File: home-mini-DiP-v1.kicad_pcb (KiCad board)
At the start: 4 copper layers, 72.4 x 70 mm, 241 parts, among them J1 FH34SRJ-16S-0.5SH_50_, J2 1775443-2, J3 XMOS JTAG, J4 XTAG DEV, J5 Conn_01x05, Q1 LBSS138WT1G, Q2 LBSS138WT1G, Q3 BC847B, SW2 BOOT, U1 AP22802AW5-7, U10 SN74LVC125APWR, U11 TLV73333PDBVR, U13 TLV320AIC3204IRHBR, U14 TPA6211A1DGNR, U2 MPR121QR2, U3 TPS62827DMQR, U4 TPS62065DSGR, U5 ME6211C18M5G-N, U6 ESP32-S3R8, U7 W25Q128JVSIQ, U8 XU316-1024-QF60B-C24​, U9 W25Q32JVSSIQ, X1 24MHz 12pF, Y1 40MHz

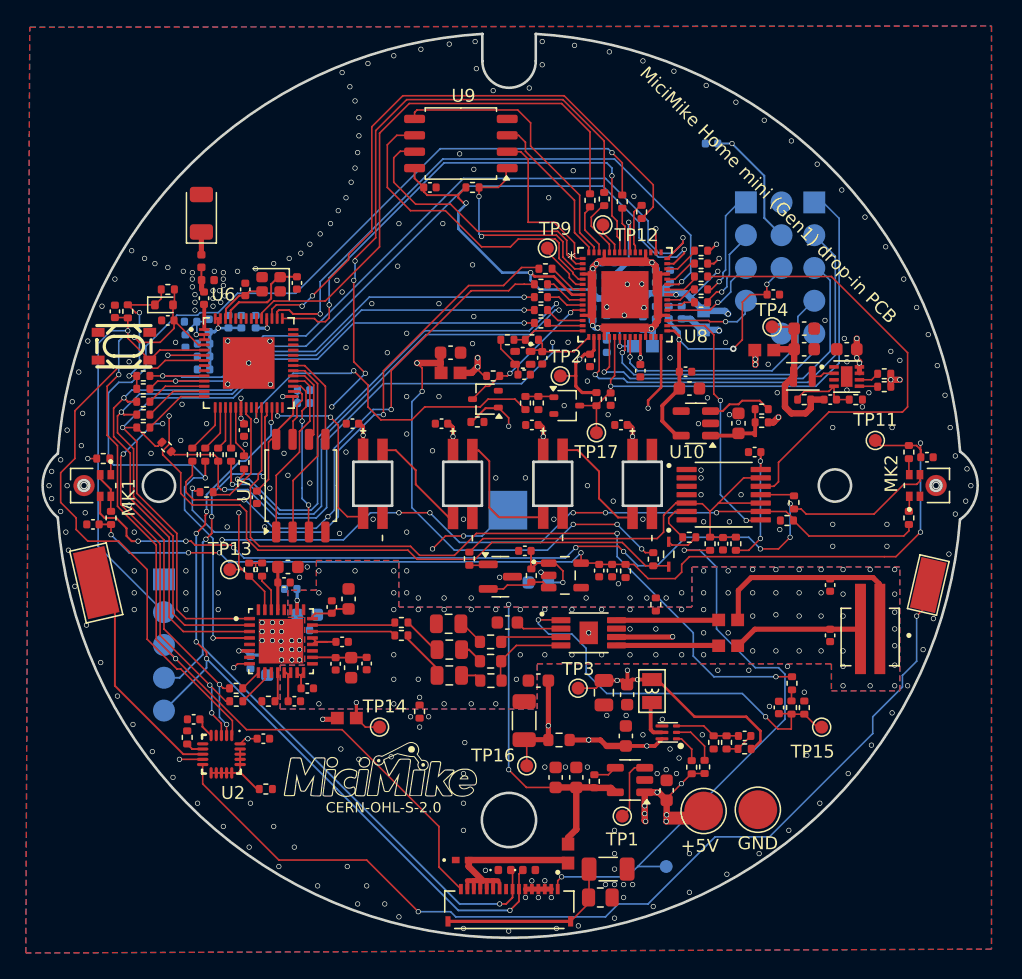
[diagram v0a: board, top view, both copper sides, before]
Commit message: layout optimization for touch pads
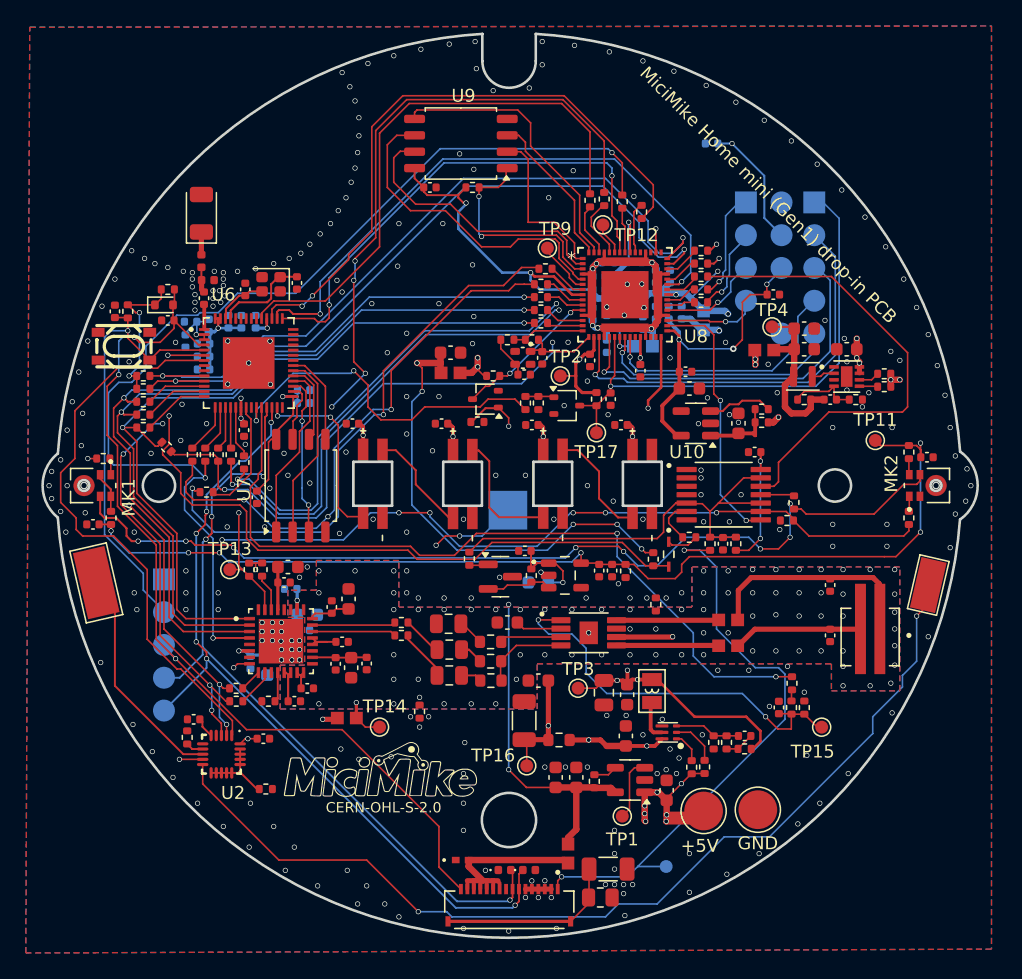
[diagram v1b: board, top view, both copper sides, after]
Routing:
- net GND: vias 301 -> 291
